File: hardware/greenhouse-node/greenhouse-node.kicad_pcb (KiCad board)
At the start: 2 copper layers, 90.2 x 69.8 mm, 49 parts, among them J1 Conn_01x12_Male, J2 Conn_01x02_Male, J3 Conn_01x02_Male, J4 Conn_01x02_Male, J5 Conn_01x04_Male, J6 RX_PinHeader_1x04_P2.54mm, J7 TX_PinHeader_1x04_P2.54mm, J8 Conn_01x02_Male, Q1 BC549C, Q2 BC549C, Q3 BC549C, Q4 IRF9530N, Q5 IRF530N, Q6 IRF9530N, Q7 IRF530N, Q8 BC549C, Q9 BC549C, U1 ATtiny84A-P, U2 L7805, U3 74HC595

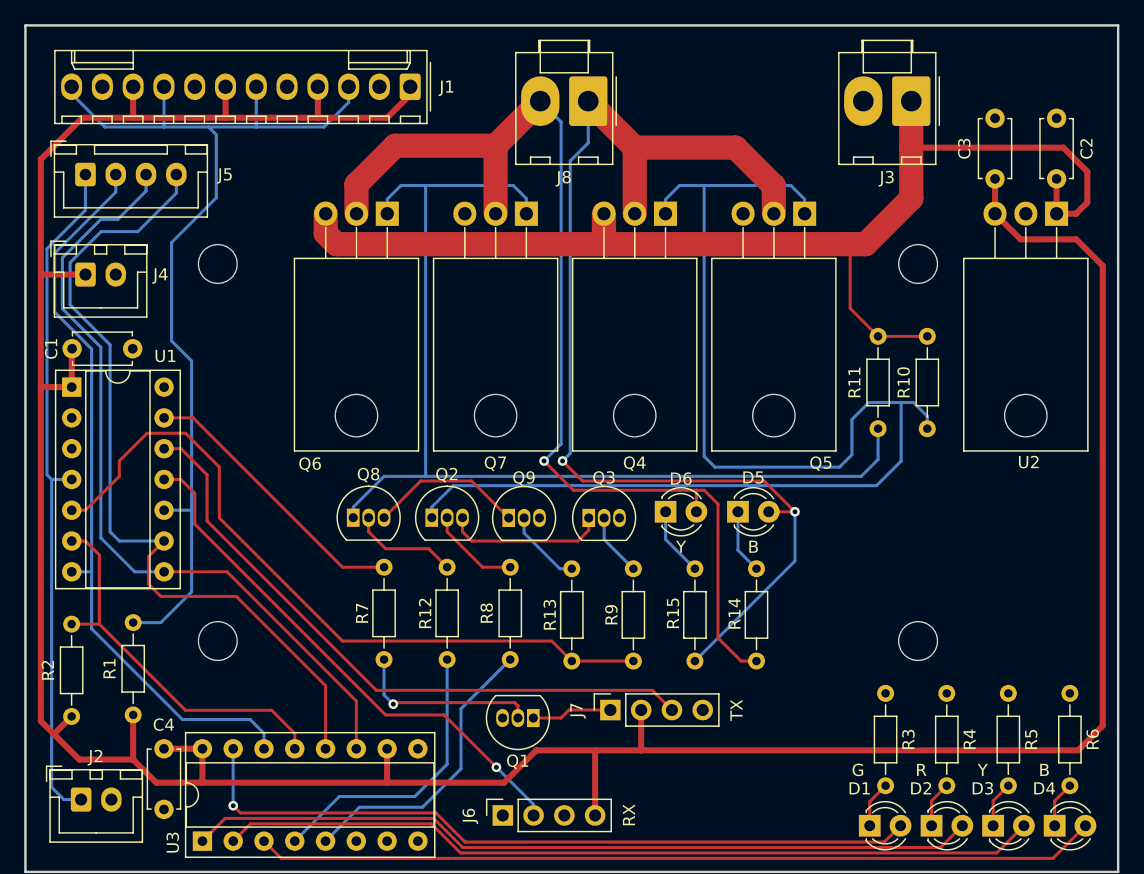
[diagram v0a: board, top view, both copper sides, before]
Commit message: Add cap and diode
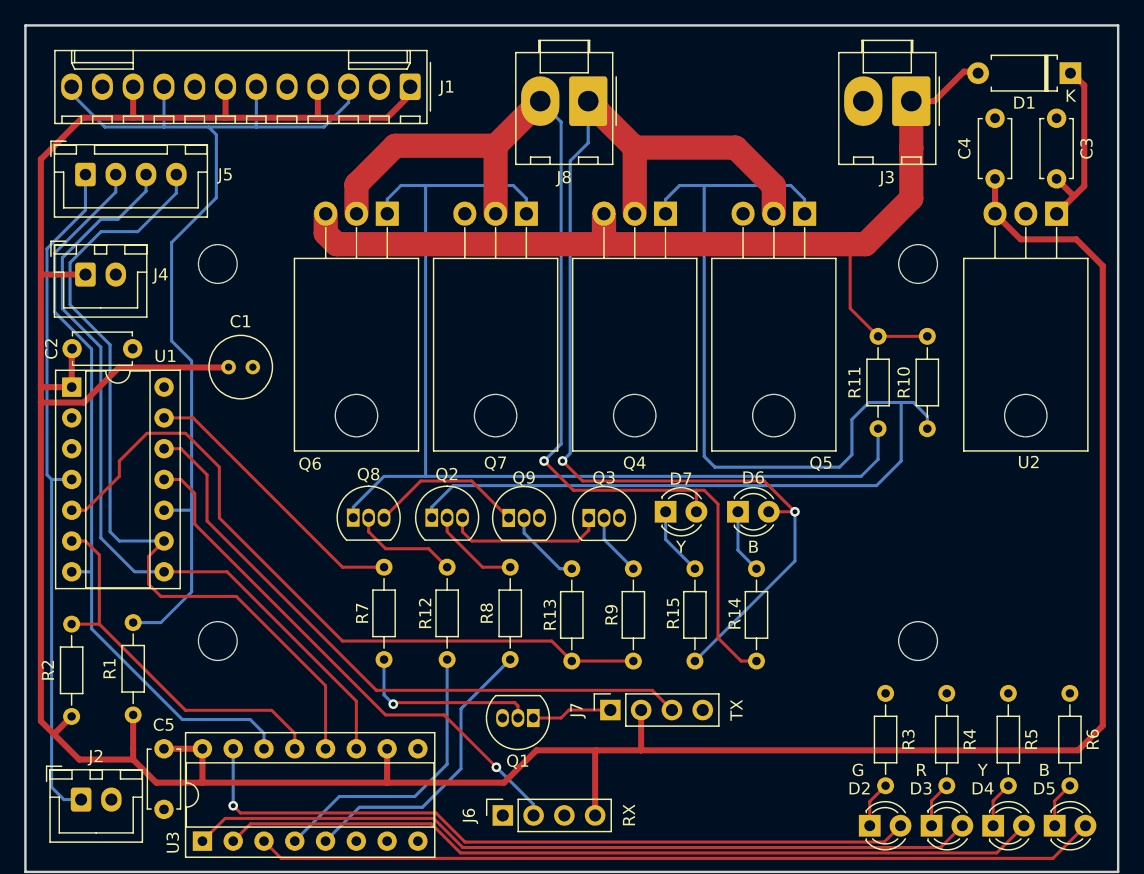
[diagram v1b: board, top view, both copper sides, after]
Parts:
- added C1: 100uF, Capacitor_THT:C_Radial_D5.0mm_H7.0mm_P2.00mm, F.Cu at (145.0, 73.9)
- added D1: D, Diode_THT:D_A-405_P7.62mm_Horizontal, F.Cu at (214.5, 49.7)
- renumbered C1 to C2, C2 to C3, C3 to C4, C4 to C5, D1 to D2, D2 to D3, D3 to D4, D4 to D5, D5 to D6, D6 to D7
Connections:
- C3 pad 2: +10V -> Net-(C3-Pad2)
- U2 pad 1: +10V -> Net-(C3-Pad2)
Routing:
- net +10V: track 99.6 -> 82.4 mm
- net +5V: track 262.5 -> 279.2 mm
- net Net-(C3-Pad2): track 0.00 -> 15.2 mm

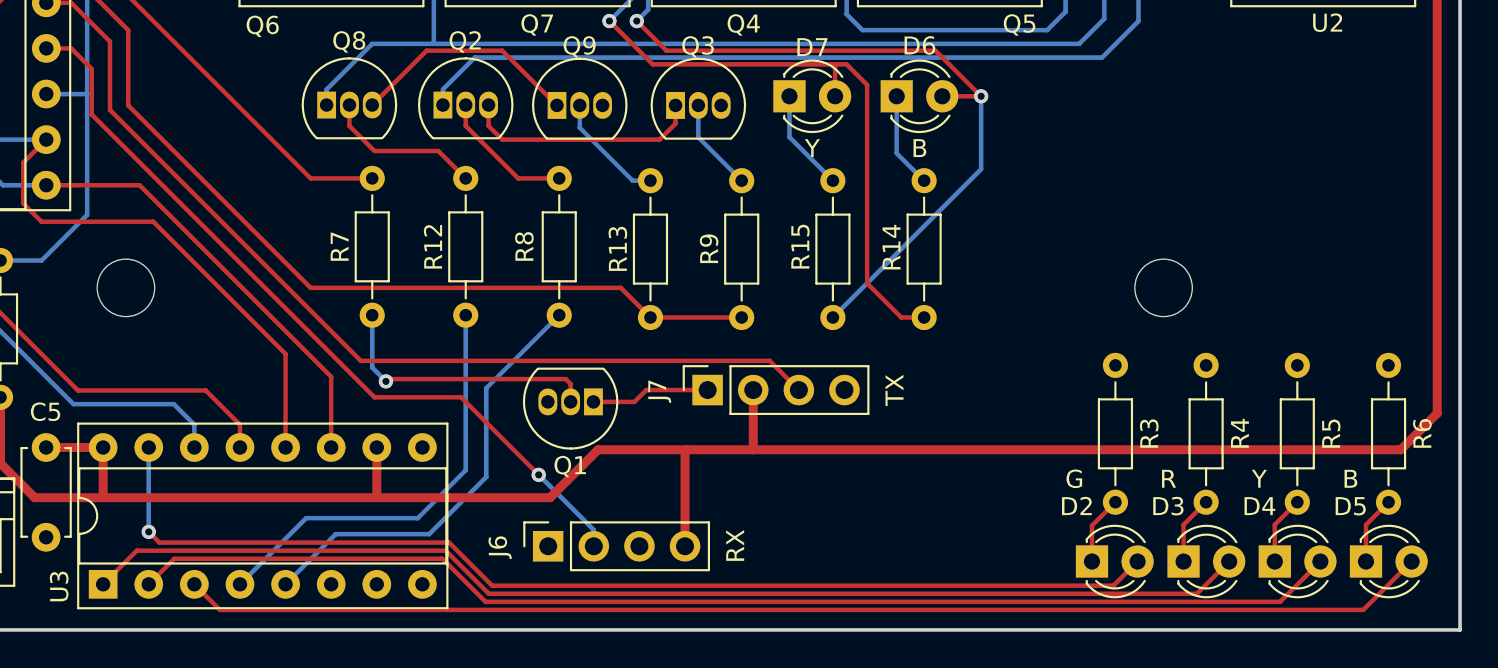
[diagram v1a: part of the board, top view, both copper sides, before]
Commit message: Reposition RX/TX
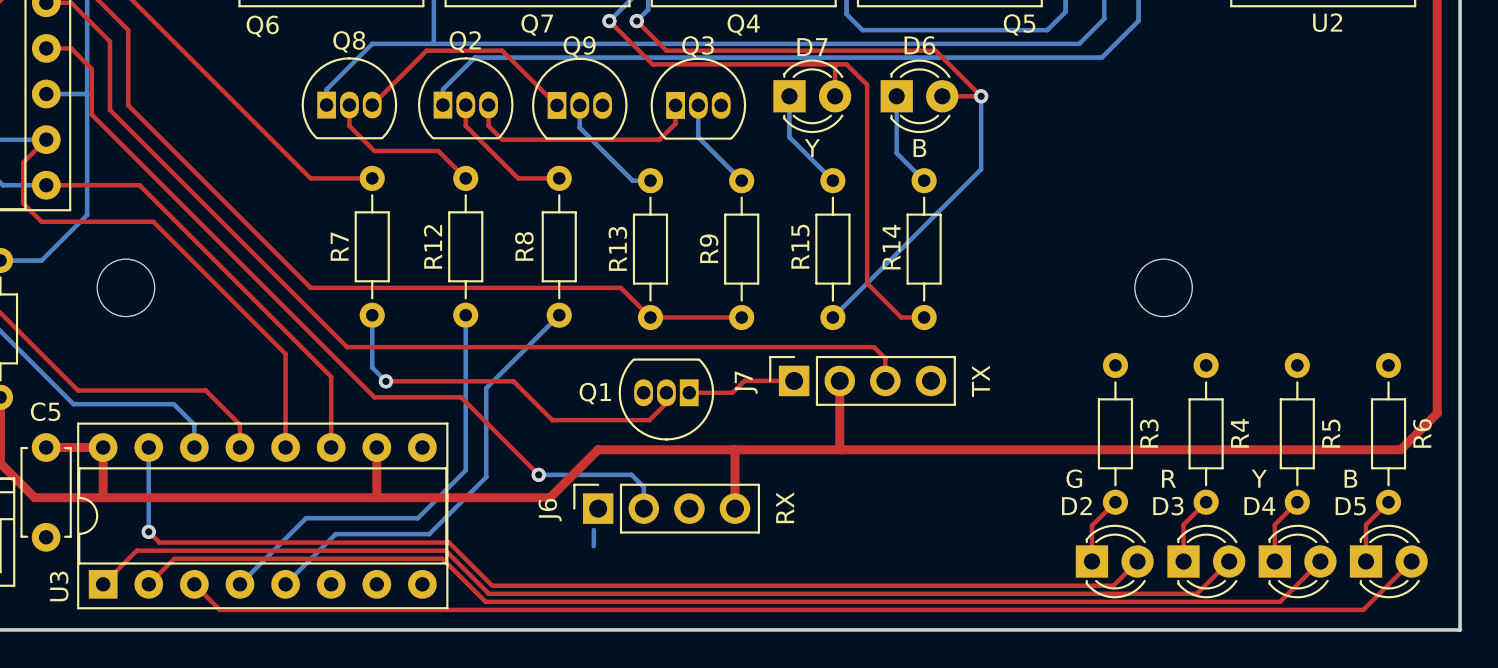
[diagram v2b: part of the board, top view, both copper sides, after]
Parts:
- moved Q1 5.36 mm to (175.5, 102.4)
- moved J7 4.84 mm to (181.4, 101.7)
- moved J6 3.48 mm to (170.4, 108.8)
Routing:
- net Net-(Q1-Pad2): track 15.5 -> 21.5 mm
- net /RAD_TX: track 53.1 -> 58.4 mm
- net /RAD_RX: track 44.0 -> 46.1 mm
- net +5V: track 279.2 -> 277.6 mm
- net GND: track 0.00 -> 0.91 mm
- net Net-(J7-Pad1): track 6.63 -> 6.12 mm
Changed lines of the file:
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@@
   )
   (footprint "Connector_PinSocket_2.54mm:PinSocket_1x04_P2.54mm_Vertical" (layer "F.Cu")
-    (at 167.66 110.91 90)
+    (at 170.444 108.814 90)
     (descr "Through hole straight socket strip, 1x04, 2.54mm pitch, single row (from Kicad 4.0.7), script generated")
     (tags "Through hole socket strip THT 1x04 2.54mm single row")
@@
   )
   (footprint "Connector_PinSocket_2.54mm:PinSocket_1x04_P2.54mm_Vertical" (layer "F.Cu")
-    (at 176.54 102.21 90)
+    (at 181.356 101.702 90)
     (descr "Through hole straight socket strip, 1x04, 2.54mm pitch, single row (from Kicad 4.0.7), script generated")
     (tags "Through hole socket strip THT 1x04 2.54mm single row")
@@
   )
   (footprint "Package_TO_SOT_THT:TO-92_Inline" (layer "F.Cu")
-    (at 170.18 102.87 180)
+    (at 175.514 102.362 180)
     (descr "TO-92 leads in-line, narrow, oval pads, drill 0.75mm (see NXP sot054_po.pdf)")
     (tags "to-92 sc-43 sc-43a sot54 PA33 transistor")
@@
     (property "Sheetname" "")
     (attr through_hole)
-    (fp_text reference "Q1" (at 1.27 -3.56) (layer "F.SilkS")
+    (fp_text reference "Q1" (at 5.207 0) (layer "F.SilkS")
       (effects (font (size 1 1) (thickness 0.15)))
     )
@@
   (segment (start 158.115 108.204) (end 142.875 108.204) (width 0.5) (layer "F.Cu") (net 1))
   (segment (start 158.115 53.34) (end 160.02 51.435) (width 0.5) (layer "F.Cu") (net 1))
-  (segment (start 175.387 105.537) (end 170.433978 105.537) (width 0.5) (layer "F.Cu") (net 1))
   (segment (start 137.16 50.78) (end 137.16 53.34) (width 0.5) (layer "F.Cu") (net 1))
-  (segment (start 179.07 105.537) (end 215.138 105.537) (width 0.5) (layer "F.Cu") (net 1))
   (segment (start 152.4 53.34) (end 158.115 53.34) (width 0.5) (layer "F.Cu") (net 1))
   (segment (start 210.393986 63.368986) (end 208.28 61.255) (width 0.5) (layer "F.Cu") (net 1))
+  (segment (start 178.064 108.814) (end 178.064 105.547) (width 0.5) (layer "F.Cu") (net 1))
   (segment (start 129.54 75.438) (end 129.54 76.835) (width 0.5) (layer "F.Cu") (net 1))
   (segment (start 217.17 103.505) (end 217.17 65.559446) (width 0.5) (layer "F.Cu") (net 1))
   (segment (start 142.875 105.41) (end 142.875 108.204) (width 0.5) (layer "F.Cu") (net 1))
-  (segment (start 179.08 102.21) (end 179.08 105.527) (width 0.5) (layer "F.Cu") (net 1))
+  (segment (start 183.896 105.41) (end 184.023 105.537) (width 0.5) (layer "F.Cu") (net 1))
   (segment (start 137.16 105.41) (end 137.16 106.299) (width 0.5) (layer "F.Cu") (net 1))
   (segment (start 132.715 106.299) (end 137.16 106.299) (width 0.5) (layer "F.Cu") (net 1))
@@
   (segment (start 137.16 106.299) (end 139.065 108.204) (width 0.5) (layer "F.Cu") (net 1))
   (segment (start 132.08 102.743) (end 130.683 104.14) (width 0.5) (layer "F.Cu") (net 1))
+  (segment (start 215.138 105.537) (end 184.023 105.537) (width 0.5) (layer "F.Cu") (net 1))
   (segment (start 133.096 76.835) (end 129.54 76.835) (width 0.5) (layer "F.Cu") (net 1))
   (segment (start 135.986489 73.944511) (end 133.096 76.835) (width 0.5) (layer "F.Cu") (net 1))
@@
   (segment (start 129.54 75.438) (end 129.54 56.769) (width 0.5) (layer "F.Cu") (net 1))
   (segment (start 132.09 75.565) (end 132.09 72.425) (width 0.5) (layer "F.Cu") (net 1))
-  (segment (start 179.08 105.527) (end 179.07 105.537) (width 0.5) (layer "F.Cu") (net 1))
   (segment (start 129.54 103.124) (end 130.556 104.14) (width 0.5) (layer "F.Cu") (net 1))
   (segment (start 139.065 108.204) (end 142.875 108.204) (width 0.5) (layer "F.Cu") (net 1))
-  (segment (start 175.28 110.91) (end 175.28 105.644) (width 0.5) (layer "F.Cu") (net 1))
+  (segment (start 183.896 101.702) (end 183.896 105.41) (width 0.5) (layer "F.Cu") (net 1))
   (segment (start 130.556 104.14) (end 132.715 106.299) (width 0.5) (layer "F.Cu") (net 1))
+  (segment (start 178.064 105.547) (end 178.054 105.537) (width 0.5) (layer "F.Cu") (net 1))
   (segment (start 214.97954 63.368986) (end 210.393986 63.368986) (width 0.5) (layer "F.Cu") (net 1))
   (segment (start 144.78 50.78) (end 144.78 53.34) (width 0.5) (layer "F.Cu") (net 1))
   (segment (start 133.223 66.277) (end 129.65 66.277) (width 0.5) (layer "F.Cu") (net 1))
+  (segment (start 184.023 105.537) (end 178.054 105.537) (width 0.5) (layer "F.Cu") (net 1))
+  (segment (start 178.054 105.537) (end 170.433978 105.537) (width 0.5) (layer "F.Cu") (net 1))
   (segment (start 145.034 73.914) (end 145.003489 73.944511) (width 0.5) (layer "F.Cu") (net 1))
-  (segment (start 175.28 105.644) (end 175.387 105.537) (width 0.5) (layer "F.Cu") (net 1))
-  (segment (start 179.07 105.537) (end 175.387 105.537) (width 0.5) (layer "F.Cu") (net 1))
   (segment (start 158.115 105.41) (end 158.115 108.204) (width 0.5) (layer "F.Cu") (net 1))
+  (segment (start 170.2 110.002) (end 170.2 110.91) (width 0.25) (layer "B.Cu") (net 2))
   (segment (start 142.24 86.868) (end 142.24 84.328) (width 0.25) (layer "F.Cu") (net 3))
   (segment (start 167.132 106.934) (end 162.814 102.616) (width 0.25) (layer "F.Cu") (net 3))
@@
   (segment (start 141.097 83.185) (end 139.71 83.185) (width 0.25) (layer "F.Cu") (net 3))
   (via (at 167.132 106.934) (size 0.8) (drill 0.4) (layers "F.Cu" "B.Cu") (net 3))
-  (segment (start 170.2 110.002) (end 170.2 110.91) (width 0.25) (layer "B.Cu") (net 3))
-  (segment (start 167.132 106.934) (end 170.2 110.002) (width 0.25) (layer "B.Cu") (net 3))
+  (segment (start 172.306081 106.934) (end 172.984 107.611919) (width 0.25) (layer "B.Cu") (net 3))
+  (segment (start 167.132 106.934) (end 172.306081 106.934) (width 0.25) (layer "B.Cu") (net 3))
+  (segment (start 172.984 107.611919) (end 172.984 108.814) (width 0.25) (layer "B.Cu") (net 3))
   (segment (start 154.432 90.424) (end 142.113 78.105) (width 0.25) (layer "F.Cu") (net 4))
   (segment (start 157.861 90.424) (end 154.432 90.424) (width 0.25) (layer "F.Cu") (net 4))
@@
   (segment (start 134.8205 54.102) (end 139.7 54.102) (width 0.25) (layer "B.Cu") (net 17))
   (segment (start 139.446 94.996) (end 137.16 94.996) (width 0.25) (layer "B.Cu") (net 17))
+  (segment (start 156.464 99.822) (end 143.256 86.614) (width 0.25) (layer "F.Cu") (net 18))
+  (segment (start 185.801 99.822) (end 156.464 99.822) (width 0.25) (layer "F.Cu") (net 18))
+  (segment (start 143.256 86.614) (end 143.256 82.804) (width 0.25) (layer "F.Cu") (net 18))
+  (segment (start 141.097 80.645) (end 139.71 80.645) (width 0.25) (layer "F.Cu") (net 18))
+  (segment (start 186.436 101.702) (end 186.436 100.457) (width 0.25) (layer "F.Cu") (net 18))
+  (segment (start 186.436 100.457) (end 185.801 99.822) (width 0.25) (layer "F.Cu") (net 18))
   (segment (start 143.256 82.804) (end 141.097 80.645) (width 0.25) (layer "F.Cu") (net 18))
-  (segment (start 141.097 80.645) (end 139.71 80.645) (width 0.25) (layer "F.Cu") (net 18))
-  (segment (start 181.62 102.21) (end 179.994 100.584) (width 0.25) (layer "F.Cu") (net 18))
-  (segment (start 179.994 100.584) (end 157.226 100.584) (width 0.25) (layer "F.Cu") (net 18))
-  (segment (start 143.256 86.614) (end 143.256 82.804) (width 0.25) (layer "F.Cu") (net 18))
-  (segment (start 157.226 100.584) (end 143.256 86.614) (width 0.25) (layer "F.Cu") (net 18))
   (segment (start 146.012449 110.706449) (end 162.142885 110.706449) (width 0.25) (layer "F.Cu") (net 19))
   (segment (start 199.136649 113.105951) (end 200.4826 111.76) (width 0.25) (layer "F.Cu") (net 19))
@@
   (segment (start 187.066 85.852) (end 187.066 89.022) (width 0.25) (layer "B.Cu") (net 27))
   (segment (start 187.066 89.022) (end 188.595 90.551) (width 0.25) (layer "B.Cu") (net 27))
-  (segment (start 173.126 102.21) (end 176.54 102.21) (width 0.25) (layer "F.Cu") (net 32))
-  (segment (start 172.466 102.87) (end 173.126 102.21) (width 0.25) (layer "F.Cu") (net 32))
-  (segment (start 170.18 102.87) (end 172.466 102.87) (width 0.25) (layer "F.Cu") (net 32))
+  (segment (start 177.927 102.362) (end 178.587 101.702) (width 0.25) (layer "F.Cu") (net 32))
+  (segment (start 178.587 101.702) (end 181.356 101.702) (width 0.25) (layer "F.Cu") (net 32))
+  (segment (start 175.514 102.362) (end 177.927 102.362) (width 0.25) (layer "F.Cu") (net 32))
   (segment (start 153.035 113.03) (end 155.829 110.236) (width 0.25) (layer "B.Cu") (net 34))
   (segment (start 155.829 110.236) (end 161.036 110.236) (width 0.25) (layer "B.Cu") (net 34))
@@
   (segment (start 160.401 109.347) (end 154.178 109.347) (width 0.25) (layer "B.Cu") (net 35))
   (segment (start 154.178 109.347) (end 150.495 113.03) (width 0.25) (layer "B.Cu") (net 35))
-  (segment (start 168.64 101.6) (end 168.91 101.87) (width 0.25) (layer "F.Cu") (net 36))
-  (segment (start 168.91 101.87) (end 168.91 102.87) (width 0.25) (layer "F.Cu") (net 36))
-  (segment (start 158.75 101.6) (end 168.64 101.6) (width 0.25) (layer "F.Cu") (net 36))
-  (segment (start 158.623 101.727) (end 158.75 101.6) (width 0.25) (layer "F.Cu") (net 36))
+  (segment (start 174.244 102.942666) (end 174.244 102.362) (width 0.25) (layer "F.Cu") (net 36))
+  (segment (start 173.300666 103.886) (end 174.244 102.942666) (width 0.25) (layer "F.Cu") (net 36))
+  (segment (start 158.623 101.727) (end 165.735 101.727) (width 0.25) (layer "F.Cu") (net 36))
+  (segment (start 165.735 101.727) (end 167.894 103.886) (width 0.25) (layer "F.Cu") (net 36))
+  (segment (start 167.894 103.886) (end 173.300666 103.886) (width 0.25) (layer "F.Cu") (net 36))
   (via (at 158.623 101.727) (size 0.8) (drill 0.4) (layers "F.Cu" "B.Cu") (net 36))
   (segment (start 157.861 100.965) (end 157.861 98.044) (width 0.25) (layer "B.Cu") (net 36))
